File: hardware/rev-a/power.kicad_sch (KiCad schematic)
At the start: 34 parts, among them J1 SOLAR, J2 LiFePO4, Q1 AO3401A, Q2 AO3401A, U1 BQ25570, U2 TPS61099

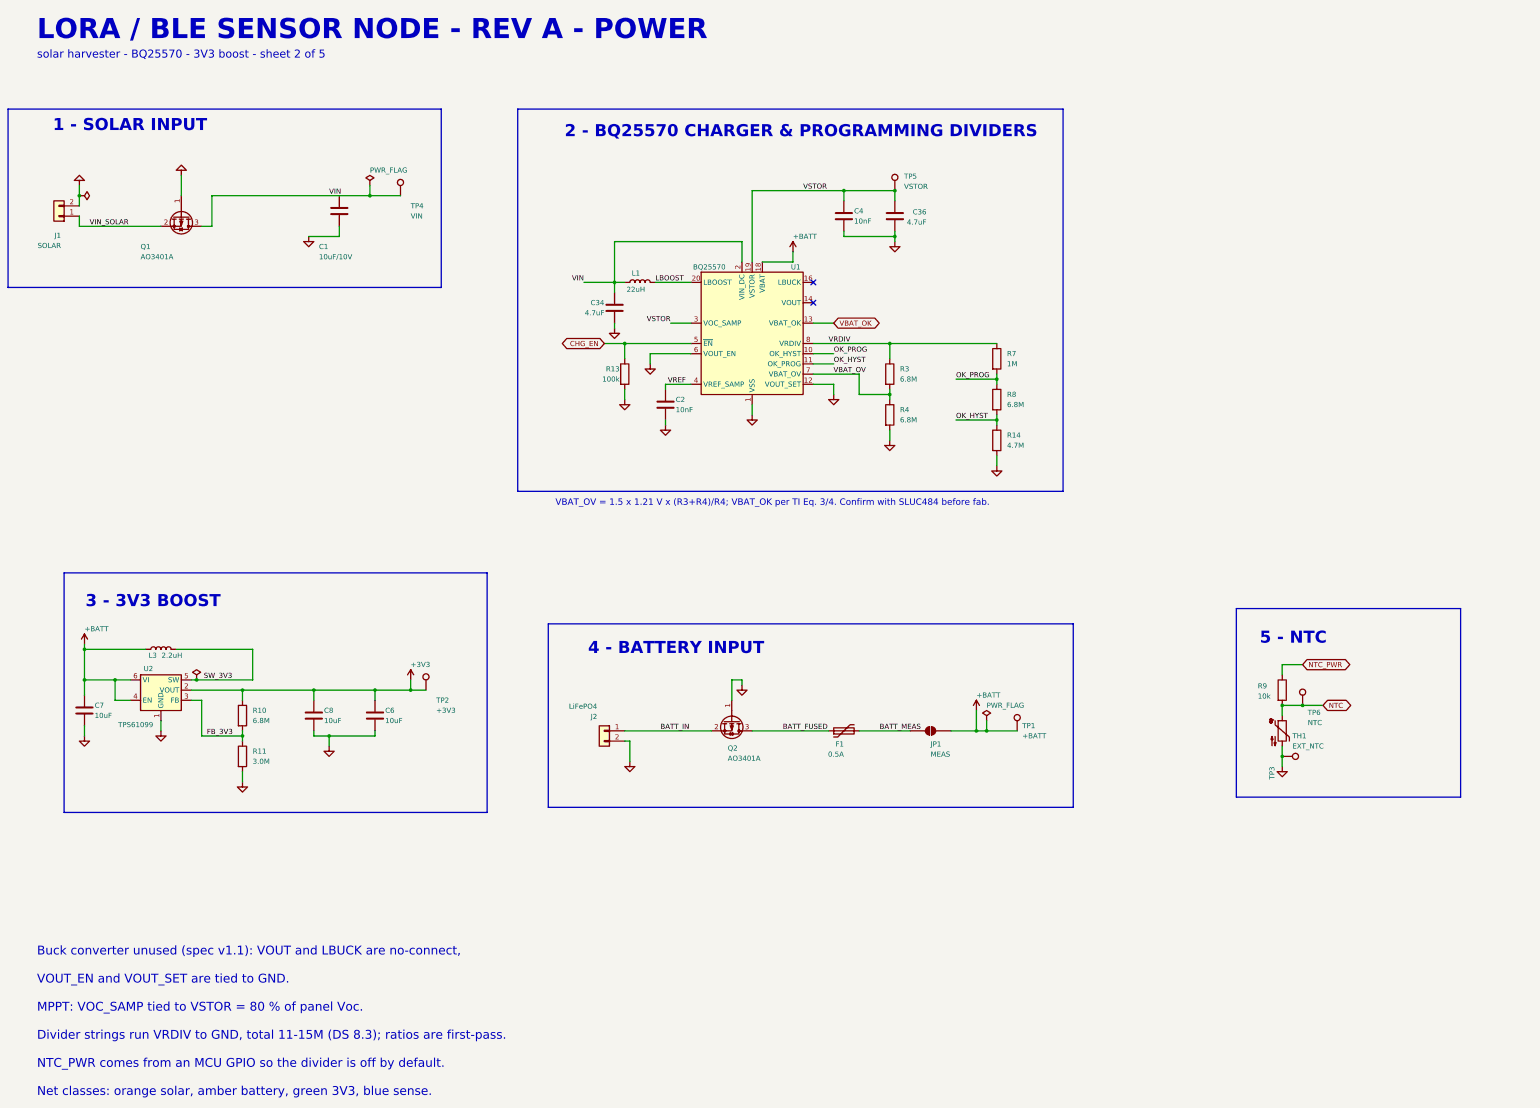
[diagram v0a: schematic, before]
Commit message: Schematic: cosmetic pass over the sheet artwork
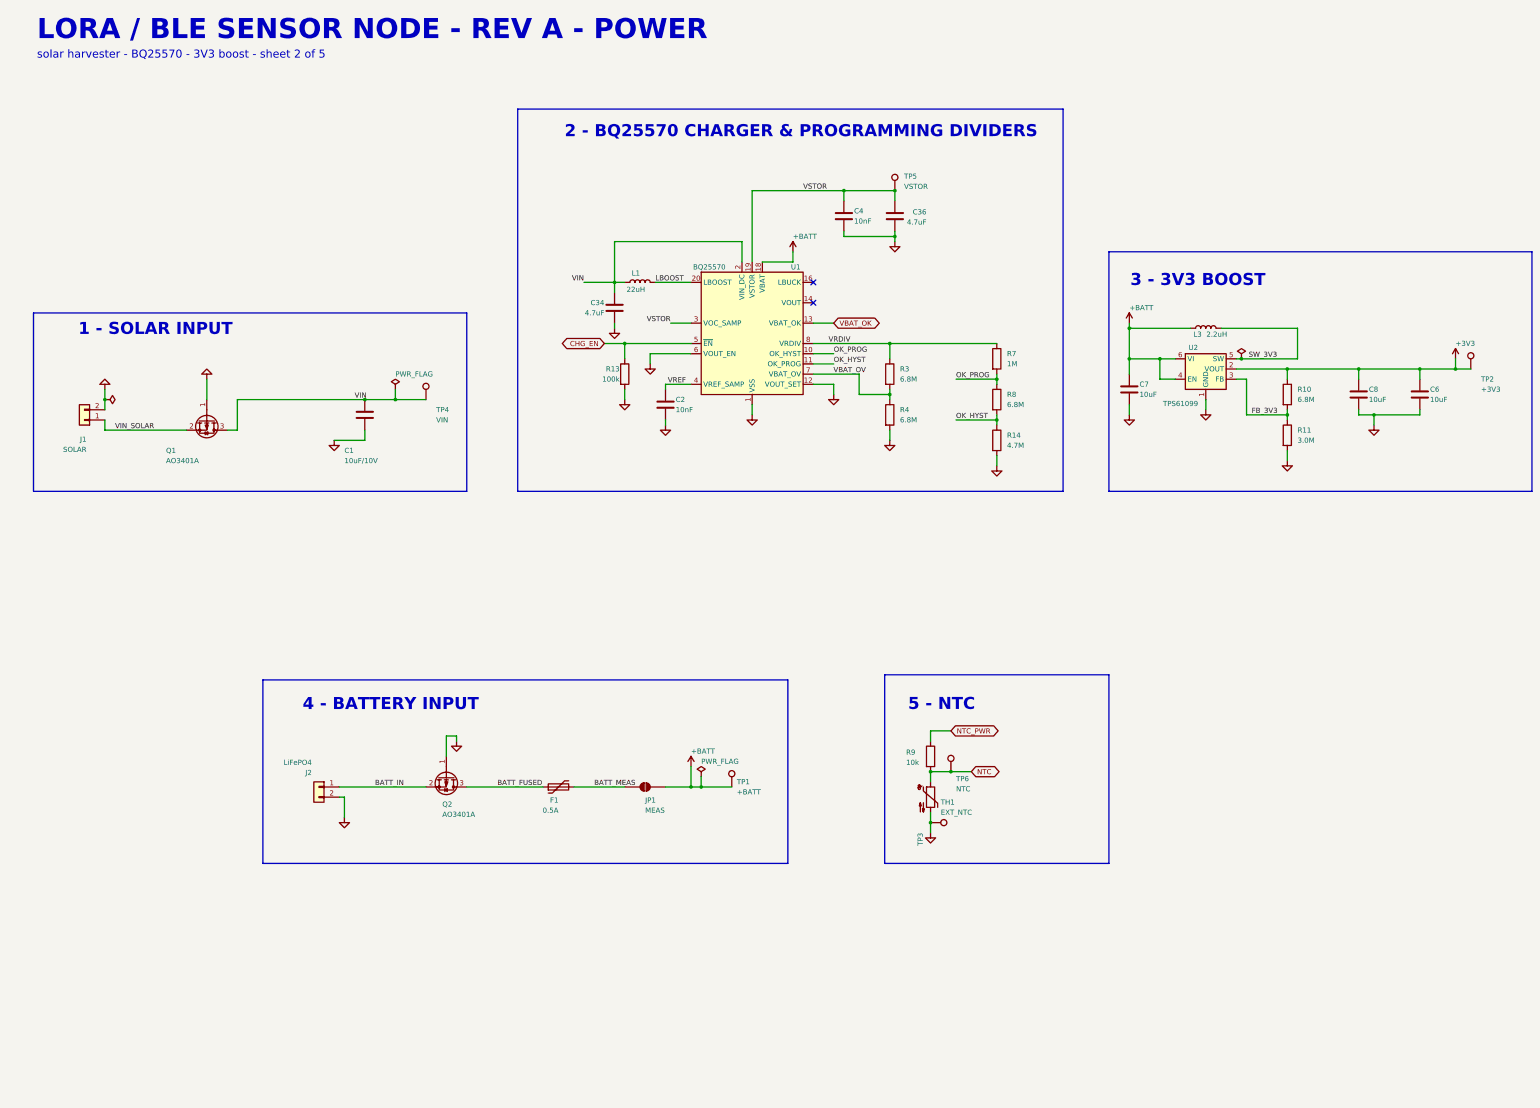
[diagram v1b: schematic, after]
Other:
- note removed: "Buck converter unused (spec v1.1): VOUT and LBUCK are no-connect,"
- note removed: "Divider strings run VRDIV to GND, total 11-15M (DS 8.3); ratios are first-pass."
- note removed: "MPPT: VOC_SAMP tied to VSTOR = 80 % of panel Voc."
- note removed: "NTC_PWR comes from an MCU GPIO so the divider is off by default."
- note removed: "Net classes: orange solar, amber battery, green 3V3, blue sense."
- note removed: "VBAT_OV = 1.5 x 1.21 V x (R3+R4)/R4; VBAT_OK per TI Eq. 3/4. Confirm with SLUC484 before fab."
- note removed: "VOUT_EN and VOUT_SET are tied to GND."
- moved on the sheet: C1, C6, C7, C8, F1, J1, J2, JP1, L3, Q1, Q2, R10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
